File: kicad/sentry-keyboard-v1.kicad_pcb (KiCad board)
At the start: 2 copper layers, 315 x 121 mm, 272 parts, among them J1 USB_C_Receptacle_USB2.0, J4 AVR-ISP-6, SW1 Reset, SW2 RotaryEncoder_Switch, U1 ATmega32U4-AU, U3 PRTR5V0U2X, Y1 16Mhz

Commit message: Align row 5
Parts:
- moved D73 5.63 mm to (73.3, 192.0)
- moved D99 5.27 mm to (271.3, 194.2)
- moved D88 5.02 mm to (99.7, 174.2)
- moved D89 5.02 mm to (119.2, 174.8)
- moved D90 5.02 mm to (138.7, 174.2)
- moved D91 5.02 mm to (158.2, 174.2)
- moved D92 5.02 mm to (177.2, 174.2)
- moved D93 5.02 mm to (196.2, 174.8)
- moved D94 5.02 mm to (216.2, 174.2)
- moved D86 5.02 mm to (64.2, 194.2)
- moved D85 5.00 mm to (87.8, 194.2)
- moved D84 4.92 mm to (111.8, 194.2)
- moved D74 4.74 mm to (97.2, 192.0)
- moved D136 4.53 mm to (320.7, 117.2)
- moved D78 4.53 mm to (278.6, 192.5)
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
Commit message: Fix up
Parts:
- moved D105 4.07 mm to (331.8, 178.8)
- moved D71 4.07 mm to (339.1, 177.8)
- moved MXup1 4.07 mm to (331.9, 174.0)
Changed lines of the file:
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@@
 	(footprint "Keebio:SK6812-MINI-E"
 		(layer "B.Cu")
-		(at 331.825 174.75 180)
+		(at 331.825 178.819517 180)
 		(property "Reference" "D105"
 			(at 0.08 -2.1 0)
@@
 	(footprint "Kaihl hotswap:MX-Hotswap-1U"
 		(layer "B.Cu")
-		(at 331.920084 169.930483 180)
+		(at 331.920084 174 180)
 		(property "Reference" "MXup1"
 			(at 0 -3.175 0)
@@
 	(footprint "Diode_SMD:D_SOD-123"
 		(layer "B.Cu")
-		(at 339.121735 173.759199 180)
+		(at 339.121735 177.828716 180)
 		(descr "SOD-123")
 		(tags "SOD-123")

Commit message: Get row 4 placed.
Had to change the size of several switches as they were wrong.
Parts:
- MXenter1: footprint Kaihl hotswap:MX-Hotswap-1.5U -> Kaihl hotswap:MX-Hotswap-2.25U
- MXlshift1: footprint Kaihl hotswap:MX-Hotswap-2U -> Kaihl hotswap:MX-Hotswap-2.25U
- moved D70 8.13 mm to (309.7, 174.0)
- moved D106 7.43 mm to (302.2, 175.3)
- moved D88 5.04 mm to (104.6, 175.2)
- moved D62 5.00 mm to (149.8, 174.2)
- moved D89 4.51 mm to (123.7, 175.2)
- moved MXz1 4.44 mm to (104.6, 170.4)
- moved D25 4.44 mm to (80.4, 173.0)
- moved MXc1 4.34 mm to (142.7, 170.4)
- moved D65 4.32 mm to (207.1, 173.5)
- moved D64 4.31 mm to (188.0, 174.0)
- moved D90 4.24 mm to (142.8, 175.2)
- moved D63 3.88 mm to (169.0, 174.1)
- moved MXx1 3.81 mm to (123.6, 170.4)
- moved MXb1 3.78 mm to (180.8, 170.5)
- moved D93 3.74 mm to (199.9, 175.2)
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
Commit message: Place row 3
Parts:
- moved D19 5.59 mm to (76.7, 155.0)
- moved MXcaps1 3.88 mm to (68.9, 151.4)
- moved D20 3.04 mm to (102.2, 155.0)
- moved MXg1 2.68 mm to (209.4, 151.4)
- moved D21 2.38 mm to (121.9, 155.4)
- moved MXs1 2.38 mm to (114.2, 151.4)
- moved D22 2.38 mm to (140.4, 155.4), turned to 180 degrees
- moved MXd1 2.38 mm to (133.2, 151.4)
- moved MXf2 2.36 mm to (152.2, 151.3)
- moved MXk1 2.26 mm to (228.4, 151.4)
- moved D56 2.26 mm to (235.7, 155.4)
- moved MXl1 2.22 mm to (247.5, 151.4)
- moved D60 2.17 mm to (323.9, 155.3)
- moved MXa1 2.12 mm to (95.1, 151.4)
- moved MXh1 1.96 mm to (190.4, 151.4)
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
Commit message: Place row2
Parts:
- moved D49 4.91 mm to (268.0, 136.8)
- moved D133 4.91 mm to (261.2, 138.3)
- moved MXp1 4.91 mm to (261.7, 132.3)
- moved D134 4.86 mm to (280.6, 137.8)
- moved D50 4.86 mm to (287.4, 136.3)
- moved MX[1 4.86 mm to (280.8, 132.3)
- moved D132 4.57 mm to (242.1, 138.3)
- moved MXo1 4.57 mm to (242.7, 132.3)
- moved D48 4.57 mm to (250.0, 136.8)
- moved D135 4.12 mm to (300.5, 138.8)
- moved D51 4.12 mm to (307.5, 135.8)
- moved MX]1 4.12 mm to (299.8, 132.3)
- moved D131 4.08 mm to (222.6, 138.3)
- moved MXi1 4.08 mm to (223.6, 132.3)
- moved D47 4.08 mm to (230.5, 136.8)
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
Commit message: Place row 1
Fix \ footprint as it looks like 1.5u is the right size. I have to
remeasure to be sure.
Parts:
- MX\1: footprint Kaihl hotswap:MX-Hotswap-1.25U -> Kaihl hotswap:MX-Hotswap-1.5U
- moved D161 13.5 mm to (284.2, 88.2)
- moved D33 13.5 mm to (290.9, 81.0)
- moved F11 13.5 mm to (283.5, 80.6)
- moved D139 3.88 mm to (252.9, 120.0)
- moved D39 3.88 mm to (259.6, 117.8)
- moved MX0 3.88 mm to (252.3, 113.3)
- moved D137 3.78 mm to (289.6, 120.5)
- moved D138 3.78 mm to (271.1, 120.5)
- moved D41 3.78 mm to (297.3, 118.2)
- moved D40 3.78 mm to (278.4, 117.7)
- moved MX+1 3.78 mm to (290.5, 113.2)
- moved MX-1 3.78 mm to (271.4, 113.2)
- moved MXbksp1 3.66 mm to (319.1, 113.3)
- moved D140 3.60 mm to (233.4, 120.5)
- moved MX9 3.60 mm to (233.3, 113.3)
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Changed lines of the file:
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@@
 	(footprint "Keebio:SK6812-MINI-E"
 		(layer "B.Cu")
-		(at 101.175 117.75 180)
+		(at 99.53321 120.549657 180)
 		(property "Reference" "D147"
 			(at 0 -2.1 0)
@@
 	(footprint "Keebio:SK6812-MINI-E"
 		(layer "B.Cu")
-		(at 120.675 117.25 180)
+		(at 118.994906 120.059919 180)
 		(property "Reference" "D146"
 			(at 0 -2.1 0)
@@
 	(footprint "Diode_SMD:D_SOD-123"
 		(layer "B.Cu")
-		(at 329 114.5 180)
+		(at 329.180907 114.502755 180)
 		(descr "SOD-123")
 		(tags "SOD-123")
@@
 	(footprint "Diode_SMD:D_SOD-123"
 		(layer "B.Cu")
-		(at 91.15 114.5 180)
+		(at 89.382684 117.299657 180)
 		(descr "SOD-123")
 		(tags "SOD-123")
@@
 	(footprint "Diode_SMD:D_SOD-123"
 		(layer "B.Cu")
-		(at 299.85 115.5 180)
+		(at 297.257346 118.249415 180)
 		(descr "SOD-123")
 		(tags "SOD-123")
@@
 	(footprint "Keebio:SK6812-MINI-E"
 		(layer "B.Cu")
-		(at 158.675 117.25 180)
+		(at 157.0481 120.010997 180)
 		(property "Reference" "D144"
 			(at 0 -2.1 0)
@@
 	(footprint "Keebio:SK6812-MINI-E"
 		(layer "B.Cu")
-		(at 273.675 117.75 180)
+		(at 271.082346 120.499415 180)
 		(property "Reference" "D138"
 			(at 0 -2.1 0)
@@
 	(footprint "Kaihl hotswap:MX-Hotswap-1U"
 		(layer "B.Cu")
-		(at 82.58 110.5 180)
+		(at 80.812684 113.299657 180)
 		(property "Reference" "MX1"
 			(at 0 -3.175 0)
@@
 		)
 	)
-	(footprint "Kaihl hotswap:MX-Hotswap-1.25U"
+	(footprint "Kaihl hotswap:MX-Hotswap-1.5U"
 		(layer "B.Cu")
-		(at 323 132.30443 180)
+		(at 323.658 132.30443 180)
 		(property "Reference" "MX\\1"
 			(at 0 -3.175 0)
@@
 		(attr smd)
 		(fp_line
-			(start 11.90625 9.525)
-			(end -11.90625 9.525)
+			(start 14.2875 9.525)
+			(end -14.2875 9.525)
 			(stroke
 				(width 0.15)
@@
 		)
 		(fp_line
-			(start 11.90625 -9.525)
-			(end 11.90625 9.525)
+			(start 14.2875 -9.525)
+			(end 14.2875 9.525)
 			(stroke
 				(width 0.15)
@@
 		)
 		(fp_line
-			(start 11.90625 -9.525)
-			(end -11.90625 -9.525)
+			(start 14.2875 -9.525)
+			(end -14.2875 -9.525)
 			(stroke
 				(width 0.15)
@@
 		)
 		(fp_line
-			(start -11.90625 -9.525)
-			(end -11.90625 9.525)
+			(start -14.2875 -9.525)
+			(end -14.2875 9.525)
 			(stroke
 				(width 0.15)
@@
 	(footprint "Kaihl hotswap:MX-Hotswap-2U"
 		(layer "B.Cu")
-		(at 321.5 110.5 180)
+		(at 319.088253 113.25217 180)
 		(property "Reference" "MXbksp1"
 			(at 0 -3.175 0)
@@
 	(footprint "Diode_SMD:D_SOD-123"
 		(layer "B.Cu")
-		(at 330.35 135.80443 180)
+		(at 331.008 135.80443 180)
 		(descr "SOD-123")
 		(tags "SOD-123")
@@
 	(footprint "Diode_SMD:D_SOD-123"
 		(layer "B.Cu")
-		(at 223.5 115.5 180)
+		(at 222.065022 118.25853 180)
 		(descr "SOD-123")
 		(tags "SOD-123")
@@
 	(footprint "Keebio:SK6812-MINI-E"
 		(layer "B.Cu")
-		(at 138.675 117.75 180)
+		(at 137.131294 120.500852 180)
 		(property "Reference" "D145"
 			(at 0 -2.1 0)
@@
 	(footprint "Keebio:SK6812-MINI-E"
 		(layer "B.Cu")
-		(at 215.675 117.75 180)
+		(at 214.240022 120.50853 180)
 		(property "Reference" "D141"
 			(at 0 -2.1 0)
@@
 	(footprint "Kaihl hotswap:MX-Hotswap-1U"
 		(layer "B.Cu")
-		(at 255.08 110.5 180)
+		(at 252.348465 113.25853 180)
 		(property "Reference" "MX0"
 			(at 0 -3.175 0)
@@
 	(footprint "Diode_SMD:D_SOD-123"
 		(layer "B.Cu")
-		(at 127.85 114.5 180)
+		(at 126.169906 117.309919 180)
 		(descr "SOD-123")
 		(tags "SOD-123")
@@
 	(footprint "Keebio:SK6812-MINI-E"
 		(layer "B.Cu")
-		(at 292.175 117.75 180)
+		(at 289.582346 120.499415 180)
 		(property "Reference" "D137"
 			(at 0 -2.1 0)
@@
 	(footprint "Kaihl hotswap:MX-Hotswap-1U"
 		(layer "B.Cu")
-		(at 139.5 110.5 180)
+		(at 137.956294 113.250852 180)
 		(property "Reference" "MX4"
 			(at 0 -3.175 0)
@@
 	(footprint "Keebio:SK6812-MINI-E"
 		(layer "B.Cu")
-		(at 164.94729 138.813009 180)
+		(at 165.325 139.25 180)
 		(property "Reference" "D128"
 			(at 0 -2.1 0)
@@
 	(footprint "Diode_SMD:D_SOD-123"
 		(layer "B.Cu")
-		(at 243.65 115.5 180)
+		(at 241.340548 118.25853 180)
 		(descr "SOD-123")
 		(tags "SOD-123")
@@
 	(footprint "Kaihl hotswap:MX-Hotswap-1U"
 		(layer "B.Cu")
-		(at 61.915 110.54 180)
+		(at 61.706631 113.272973 180)
 		(property "Reference" "MXtilde1"
 			(at 0 -3.175 0)
@@
 	(footprint "Keebio:SK6812-MINI-E"
 		(layer "B.Cu")
-		(at 235.675 117.75 180)
+		(at 233.365548 120.50853 180)
 		(property "Reference" "D140"
 			(at 0 -2.1 0)
@@
 	(footprint "Diode_SMD:D_SOD-123"
 		(layer "B.Cu")
-		(at 110.15 114.5 180)
+		(at 108.50821 117.299657 180)
 		(descr "SOD-123")
 		(tags "SOD-123")
@@
 	(footprint "Kaihl hotswap:MX-Hotswap-1U"
 		(layer "B.Cu")
-		(at 158.66 110.5 180)
+		(at 157.0331 113.260997 180)
 		(property "Reference" "MX5"
 			(at 0 -3.175 0)
@@
 	(footprint "Keebio:SK6812-MINI-E"
 		(layer "B.Cu")
-		(at 60.675 117.25 180)
+		(at 60.466631 119.982973 180)
 		(property "Reference" "D149"
 			(at 0 -2.1 0)
@@
 	(footprint "Kaihl hotswap:MX-Hotswap-1U"
 		(layer "B.Cu")
-		(at 120.58 110.5 180)
+		(at 118.899906 113.309919 180)
 		(property "Reference" "MX3"
 			(at 0 -3.175 0)
@@
 	(footprint "Keebio:SK6812-MINI-E"
 		(layer "B.Cu")
-		(at 83.175 116.75 180)
+		(at 81.407684 119.549657 180)
 		(property "Reference" "D148"
 			(at 0 -2.1 0)
@@
 	(footprint "Diode_SMD:D_SOD-123"
 		(layer "B.Cu")
-		(at 147.65 114.5 180)
+		(at 146.106294 117.250852 180)
 		(descr "SOD-123")
 		(tags "SOD-123")
@@
 	(footprint "Diode_SMD:D_SOD-123"
 		(layer "B.Cu")
-		(at 166.65 115 180)
+		(at 165.0231 117.760997 180)
 		(descr "SOD-123")
 		(tags "SOD-123")
@@
 	(footprint "Kaihl hotswap:MX-Hotswap-1U"
 		(layer "B.Cu")
-		(at 101.5 110.5 180)
+		(at 99.85821 113.299657 180)
 		(property "Reference" "MX2"
 			(at 0 -3.175 0)
@@
 	(footprint "Diode_SMD:D_SOD-123"
 		(layer "B.Cu")
-		(at 290.85 94.5 180)
+		(at 290.85 81 180)
 		(descr "SOD-123")
 		(tags "SOD-123")
@@
 	(footprint "Keebio:SK6812-MINI-E"
 		(layer "B.Cu")
-		(at 320.675 117.25 180)
+		(at 320.855907 117.252755 180)
 		(property "Reference" "D136"
 			(at 0 -2.1 0)
@@
 	(footprint "Kaihl hotswap:MX-Hotswap-1U"
 		(layer "B.Cu")
-		(at 274 110.5 180)
+		(at 271.407346 113.249415 180)
 		(property "Reference" "MX-1"
 			(at 0 -3.175 0)
@@
 	(footprint "Keebio:SK6812-MINI-E"
 		(layer "B.Cu")
-		(at 284.175 101.75 180)
+		(at 284.175 88.25 180)
 		(property "Reference" "D161"
 			(at 0 -2.1 0)
@@
 	(footprint "Diode_SMD:D_SOD-123"
 		(layer "B.Cu")
-		(at 184.35 115 180)
+		(at 182.752431 117.760997 180)
 		(descr "SOD-123")
 		(tags "SOD-123")
@@
 	(footprint "Kaihl hotswap:MX-Hotswap-1U"
 		(layer "B.Cu")
-		(at 283.54 94.08 180)
+		(at 283.54 80.58 180)
 		(property "Reference" "F11"
 			(at 0 0.825 0)
@@
 	(footprint "Diode_SMD:D_SOD-123"
 		(layer "B.Cu")
-		(at 281 115 180)
+		(at 278.407346 117.749415 180)
 		(descr "SOD-123")
 		(tags "SOD-123")
@@
 	(footprint "Diode_SMD:D_SOD-123"
 		(layer "B.Cu")
-		(at 204.15 115 180)
+		(at 202.787697 117.704802 180)
 		(descr "SOD-123")
 		(tags "SOD-123")
@@
 	(footprint "Diode_SMD:D_SOD-123"
 		(layer "B.Cu")
-		(at 262.35 115 180)
+		(at 259.618465 117.75853 180)
 		(descr "SOD-123")
 		(tags "SOD-123")
@@
 	(footprint "Kaihl hotswap:MX-Hotswap-1U"
 		(layer "B.Cu")
-		(at 293.08 110.5 180)
+		(at 290.487346 113.249415 180)
 		(property "Reference" "MX+1"
 			(at 0 -3.175 0)
@@
 	(footprint "Kaihl hotswap:MX-Hotswap-1U"
 		(layer "B.Cu")
-		(at 235.58 110.5 180)
+		(at 233.270548 113.25853 180)
 		(property "Reference" "MX9"
 			(at 0 -3.175 0)
@@
 	(footprint "Diode_SMD:D_SOD-123"
 		(layer "B.Cu")
-		(at 69.5 115 180)
+		(at 69.291631 117.732973 180)
 		(descr "SOD-123")
 		(tags "SOD-123")
@@
 	(footprint "Keebio:SK6812-MINI-E"
 		(layer "B.Cu")
-		(at 255.675 117.25 180)
+		(at 252.943465 120.00853 180)
 		(property "Reference" "D139"
 			(at 0 -2.1 0)
@@
 	(footprint "Kaihl hotswap:MX-Hotswap-1U"
 		(layer "B.Cu")
-		(at 215.66 110.5 180)
+		(at 214.225022 113.25853 180)
 		(property "Reference" "MX8"
 			(at 0 -3.175 0)
@@
 	(footprint "Keebio:SK6812-MINI-E"
 		(layer "B.Cu")
-		(at 177.675 117.25 180)
+		(at 176.077431 120.010997 180)
 		(property "Reference" "D143"
 			(at 0 -2.1 0)
@@
 	(footprint "Keebio:SK6812-MINI-E"
 		(layer "B.Cu")
-		(at 196.175 117.25 180)
+		(at 194.812697 119.954802 180)
 		(property "Reference" "D142"
 			(at 0 -2.1 0)
@@
 	(footprint "Kaihl hotswap:MX-Hotswap-1U"
 		(layer "B.Cu")
-		(at 177.66 110.5 180)
+		(at 176.062431 113.260997 180)
 		(property "Reference" "MX6"
 			(at 0 -3.175 0)
@@
 	(footprint "Kaihl hotswap:MX-Hotswap-1U"
 		(layer "B.Cu")
-		(at 196.535 110.5348 180)
+		(at 195.172697 113.239602 180)
 		(property "Reference" "MX7"
 			(at 0 -3.175 0)
@@
 		(layer "F.Cu")
 		(pts
-			(xy 306 132.5) (xy 317 132.5)
+			(xy 306 132.5) (xy 317.5 132.5)
 		)
 		(height 0)
@@
 			(keep_text_aligned yes)
 		)
-		(gr_text "11"
-			(at 311.5 130.7 0)
+		(gr_text "11.5"
+			(at 311.75 130.7 0)
 			(layer "F.Cu")
 			(effects
@@
 		(layer "F.Cu")
 		(pts
-			(xy 329 132.5) (xy 366.5 130.625)
+			(xy 329.5 132.5) (xy 366.5 130.625)
 		)
 		(height 0)
@@
 			(keep_text_aligned yes)
 		)
-		(gr_text "37.5"
-			(at 347.75 130.7 0)
+		(gr_text "37"
+			(at 348 130.7 0)
 			(layer "F.Cu")
 			(effects

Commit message: Tune more of the switch footprints
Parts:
- moved D42 3.38 mm to (326.9, 117.0)
- moved D13 3.35 mm to (74.3, 136.1)
- moved D129 2.90 mm to (185.7, 137.1)
- moved D137 2.68 mm to (290.5, 118.0)
- moved D110 2.66 mm to (323.8, 137.2)
- moved D128 2.58 mm to (166.8, 137.1)
- moved D145 2.57 mm to (137.9, 118.1)
- moved D147 2.52 mm to (99.9, 118.1)
- moved D138 2.52 mm to (271.5, 118.0)
- moved D140 2.44 mm to (233.3, 118.1)
- moved D141 2.42 mm to (214.2, 118.1)
- moved D149 2.36 mm to (61.8, 118.0)
- moved D130 2.22 mm to (205.1, 137.1)
- moved D139 2.19 mm to (252.3, 117.9)
- moved D46 2.08 mm to (212.6, 136.1)
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
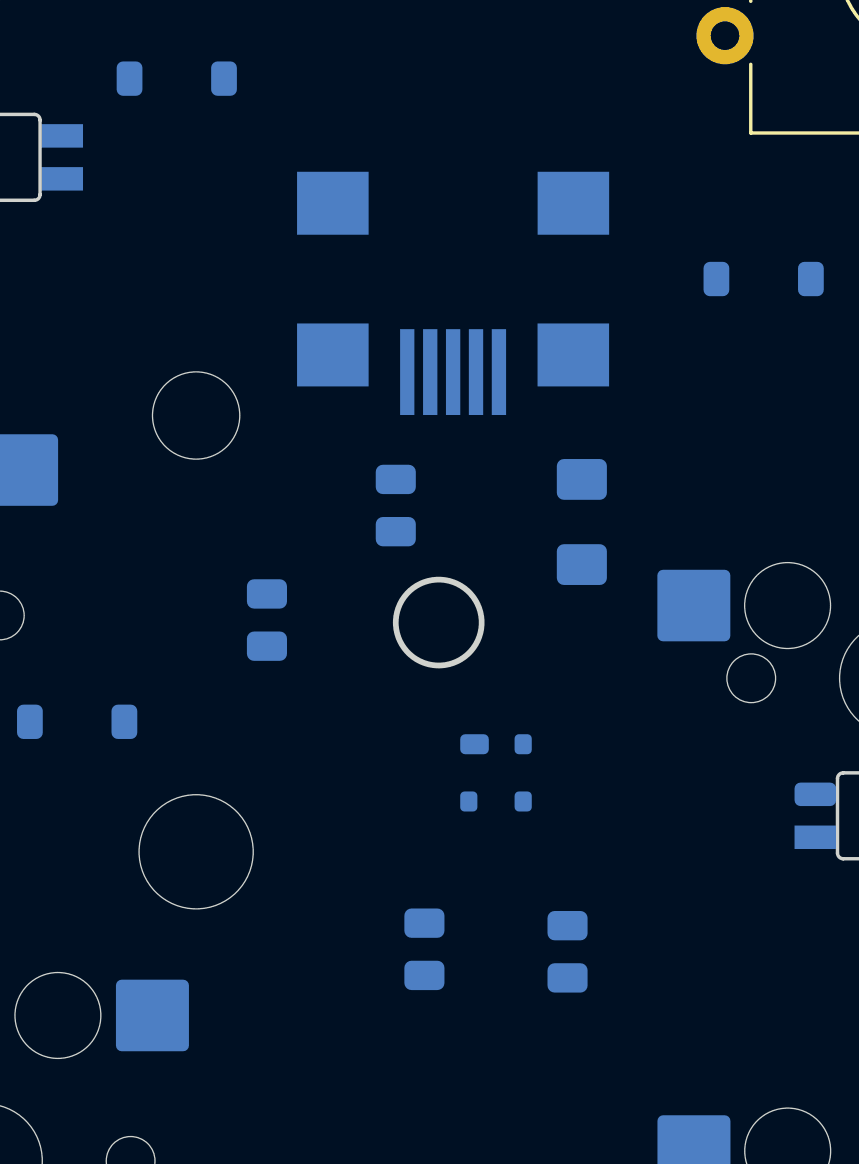
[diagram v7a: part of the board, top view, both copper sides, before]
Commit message: Simpler USB connection
The keyboard case comes with a USBC breakout card. This card contains
the 5.1K resistors, and what looks like an ESD on them. I've removed
those from the schematics, and assigned a picoblade connector, as that
is what I think the board is currently using.
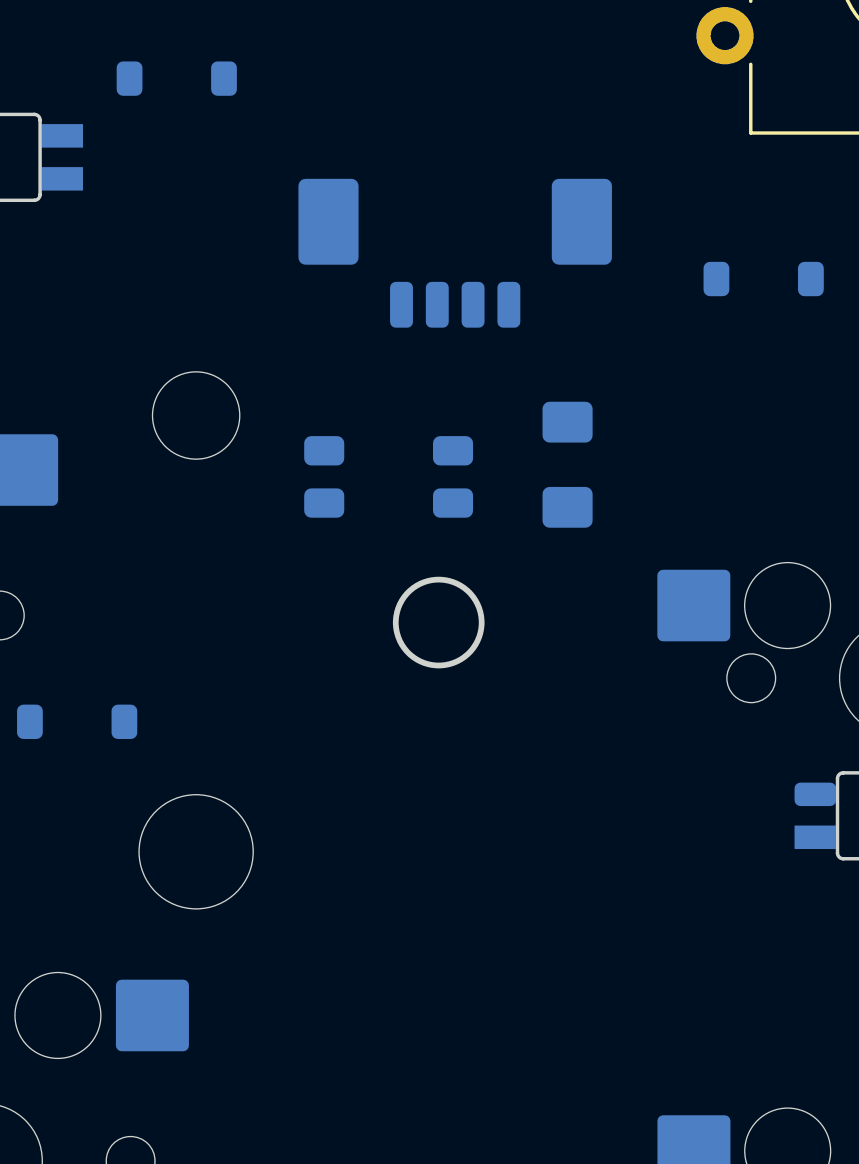
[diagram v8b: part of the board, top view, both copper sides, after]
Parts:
- removed FU1: 500mA, Fuse:Fuse_1206_3216Metric_Pad1.42x1.75mm_HandSolder
- removed J1: USB_C_Receptacle_USB2.0, Keebio:USB_miniB_HandSolder
- removed R2, R3: 5.1K, Resistor_SMD:R_0805_2012Metric
- removed R4, R5: 22, Resistor_SMD:R_0805_2012Metric
- removed U3: PRTR5V0U2X, Package_TO_SOT_SMD:SOT-143
- added FU2: 500mA, Fuse:Fuse_1206_3216Metric_Pad1.42x1.75mm_HandSolder, B.Cu at (344.0, 108.0)
- added J2: Conn_01x04, Connector_Molex:Molex_PicoBlade_53261-0471_1x04-1MP_P1.25mm_Horizontal, B.Cu at (340.1, 100.0)
- added R6: 22, Resistor_SMD:R_0805_2012Metric, B.Cu at (340.0, 108.4)
- added R7: 22, Resistor_SMD:R_0805_2012Metric, B.Cu at (335.5, 108.4)
